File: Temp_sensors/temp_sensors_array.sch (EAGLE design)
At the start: 7 parts, among them U1 SI7021, U2 SI7021, U3 HDC1080, U4 HDC1080, U5 BME280, U6 BME280

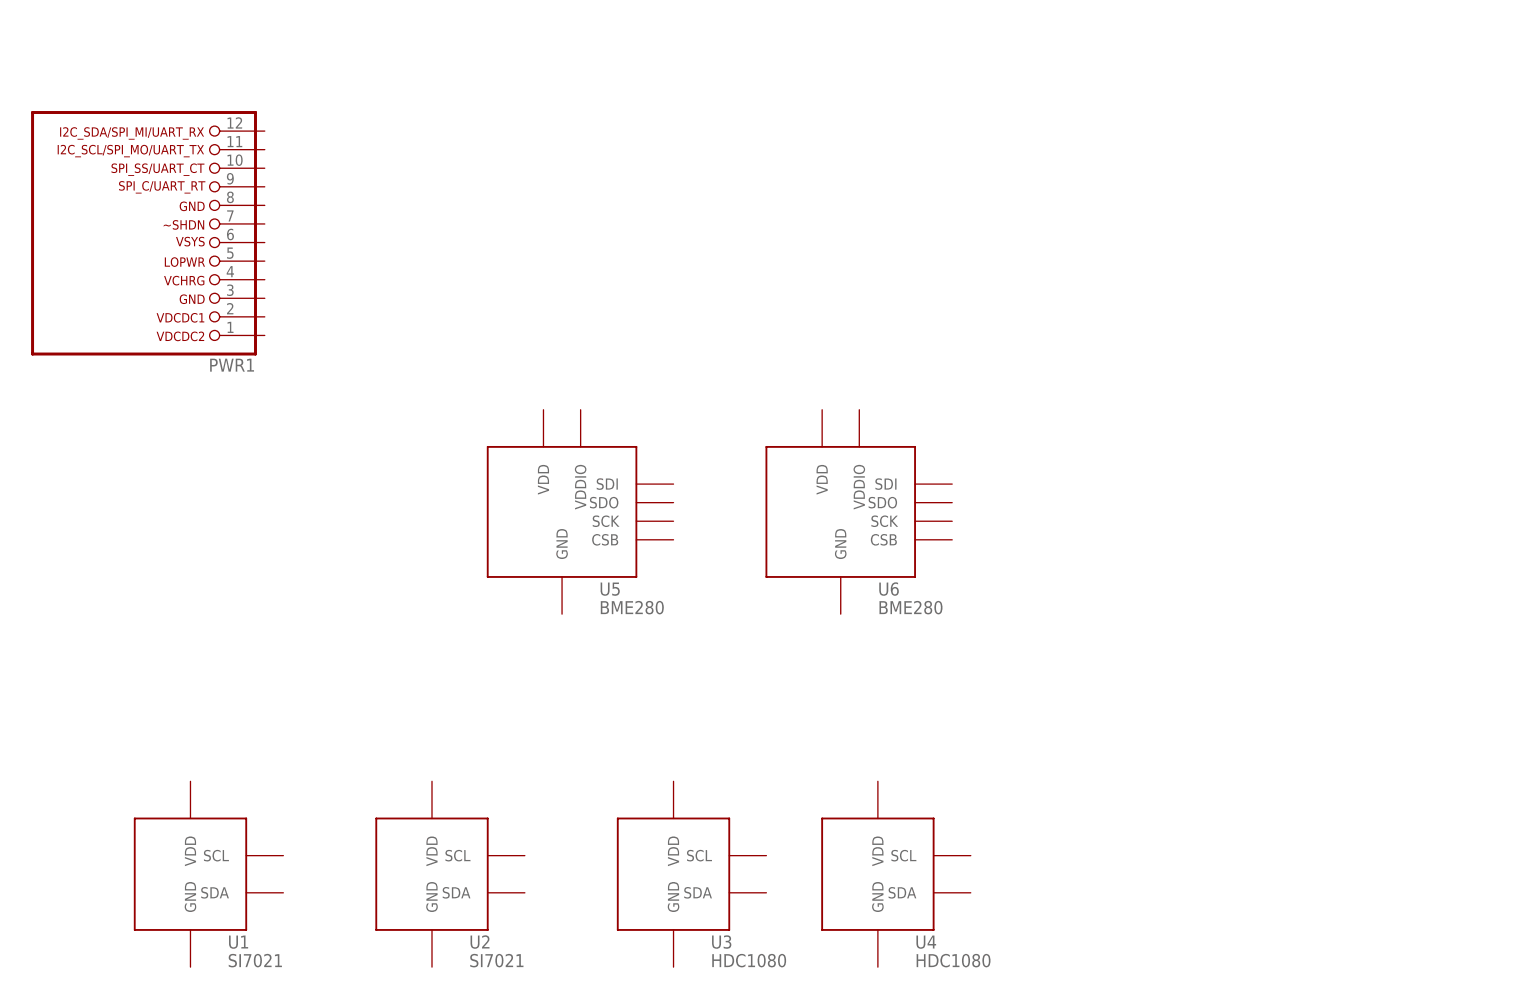
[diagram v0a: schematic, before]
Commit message: temp_array: added PCA9548APWR
Signed-off-by: malo <malo@25cmsquare.io>
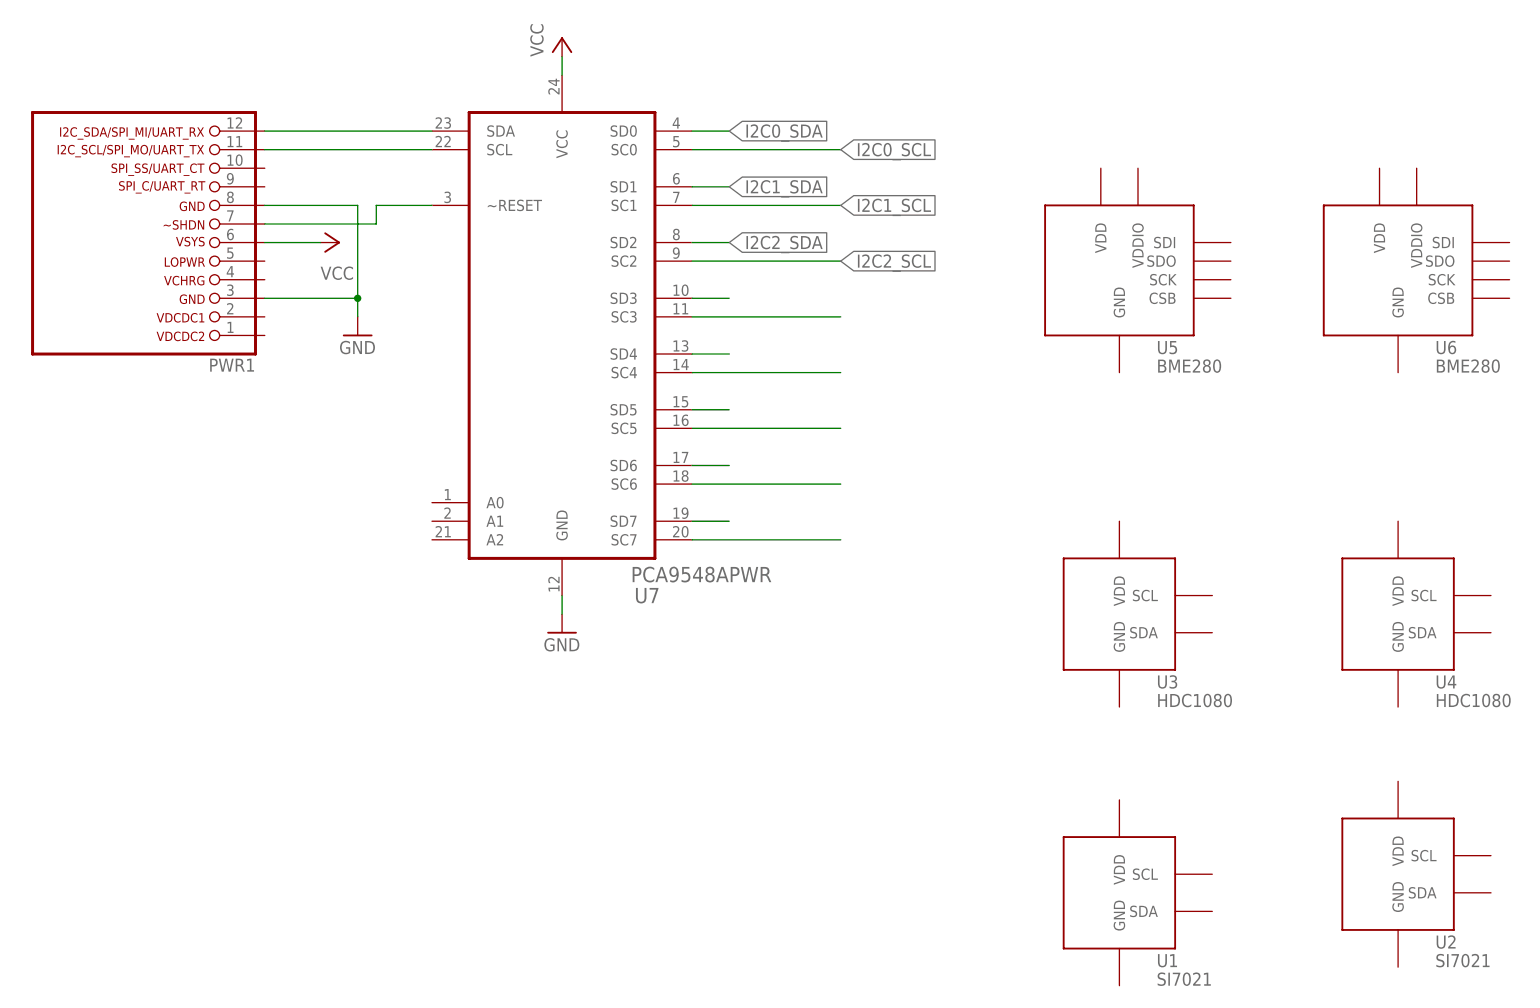
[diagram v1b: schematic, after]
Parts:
- added U7: PCA9548APWR, Texas Instruments_By_element14_Batch_1:PCA9548APWR
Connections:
- new net GND: PWR1.3, PWR1.8, U7.GND
- new net I2C0_SCL: U7.SC0
- new net I2C0_SDA: U7.SD0
- new net I2C1_SCL: U7.SC1
- new net I2C1_SDA: U7.SD1
- new net I2C2_SCL: U7.SC2
- new net I2C2_SDA: U7.SD2
- new net N$1: PWR1.12, U7.SDA
- new net N$10: U7.SD6
- new net N$11: U7.SC6
- new net N$12: U7.SD7
- new net N$13: U7.SC7
- new net N$2: PWR1.11, U7.SCL
- new net N$3: PWR1.7, U7.~RESET
- new net N$4: U7.SD3
- new net N$5: U7.SC3
- new net N$6: U7.SD4
- new net N$7: U7.SC4
- new net N$8: U7.SD5
- new net N$9: U7.SC5
- new net VCC: PWR1.6, U7.VCC
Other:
- moved on the sheet: U1, U2, U3, U4, U5, U6
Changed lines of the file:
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@@
 <part name="U5" library="25cmsquare" deviceset="BME280" device=""/>
 <part name="U6" library="25cmsquare" deviceset="BME280" device=""/>
+<part name="U7" library="Texas Instruments_By_element14_Batch_1" deviceset="PCA9548APWR" device=""/>
+<part name="GND1" library="supply1" deviceset="GND" device=""/>
+<part name="GND2" library="supply1" deviceset="GND" device=""/>
+<part name="P+1" library="supply1" deviceset="VCC" device=""/>
+<part name="P+2" library="supply1" deviceset="VCC" device=""/>
 </parts>
 <sheets>
@@
 </plain>
 <instances>
-<instance part="U1" gate="G$1" x="35.56" y="63.5"/>
-<instance part="U2" gate="G$1" x="68.58" y="63.5"/>
+<instance part="U1" gate="G$1" x="162.56" y="60.96"/>
+<instance part="U2" gate="G$1" x="200.66" y="63.5"/>
 <instance part="PWR1" gate="G$1" x="27.94" y="142.24" rot="R180"/>
 <instance part="FRAME1" gate="G$1" x="0" y="0"/>
-<instance part="U3" gate="G$1" x="101.6" y="55.88"/>
-<instance part="U4" gate="G$1" x="129.54" y="55.88"/>
-<instance part="U5" gate="G$1" x="78.74" y="96.52"/>
-<instance part="U6" gate="G$1" x="116.84" y="96.52"/>
+<instance part="U3" gate="G$1" x="162.56" y="91.44"/>
+<instance part="U4" gate="G$1" x="200.66" y="91.44"/>
+<instance part="U5" gate="G$1" x="154.94" y="129.54"/>
+<instance part="U6" gate="G$1" x="193.04" y="129.54"/>
+<instance part="U7" gate="A" x="86.36" y="129.54"/>
+<instance part="GND1" gate="1" x="58.42" y="129.54"/>
+<instance part="GND2" gate="1" x="86.36" y="88.9"/>
+<instance part="P+1" gate="VCC" x="86.36" y="170.18"/>
+<instance part="P+2" gate="VCC" x="55.88" y="142.24" smashed="yes" rot="R270">
+<attribute name="VALUE" x="53.34" y="137.16" size="1.778" layer="96"/>
+</instance>
 </instances>
 <busses>
 </busses>
 <nets>
+<net name="N$1" class="0">
+<segment>
+<pinref part="PWR1" gate="G$1" pin="12"/>
+<pinref part="U7" gate="A" pin="SDA"/>
+<wire x1="45.72" y1="157.48" x2="68.58" y2="157.48" width="0.1524" layer="91"/>
+</segment>
+</net>
+<net name="N$2" class="0">
+<segment>
+<pinref part="PWR1" gate="G$1" pin="11"/>
+<pinref part="U7" gate="A" pin="SCL"/>
+<wire x1="45.72" y1="154.94" x2="68.58" y2="154.94" width="0.1524" layer="91"/>
+</segment>
+</net>
+<net name="N$3" class="0">
+<segment>
+<pinref part="PWR1" gate="G$1" pin="7"/>
+<wire x1="45.72" y1="144.78" x2="60.96" y2="144.78" width="0.1524" layer="91"/>
+<wire x1="60.96" y1="144.78" x2="60.96" y2="147.32" width="0.1524" layer="91"/>
+<pinref part="U7" gate="A" pin="~RESET"/>
+<wire x1="60.96" y1="147.32" x2="68.58" y2="147.32" width="0.1524" layer="91"/>
+</segment>
+</net>
+<net name="GND" class="0">
+<segment>
+<pinref part="PWR1" gate="G$1" pin="3"/>
+<wire x1="45.72" y1="134.62" x2="58.42" y2="134.62" width="0.1524" layer="91"/>
+<wire x1="58.42" y1="134.62" x2="58.42" y2="132.08" width="0.1524" layer="91"/>
+<pinref part="GND1" gate="1" pin="GND"/>
+<pinref part="PWR1" gate="G$1" pin="8"/>
+<wire x1="45.72" y1="147.32" x2="58.42" y2="147.32" width="0.1524" layer="91"/>
+<wire x1="58.42" y1="147.32" x2="58.42" y2="134.62" width="0.1524" layer="91"/>
+<junction x="58.42" y="134.62"/>
+</segment>
+<segment>
+<pinref part="U7" gate="A" pin="GND"/>
+<pinref part="GND2" gate="1" pin="GND"/>
+<wire x1="86.36" y1="93.98" x2="86.36" y2="91.44" width="0.1524" layer="91"/>
+</segment>
+</net>
+<net name="VCC" class="0">
+<segment>
+<pinref part="PWR1" gate="G$1" pin="6"/>
+<pinref part="P+2" gate="VCC" pin="VCC"/>
+<wire x1="45.72" y1="142.24" x2="53.34" y2="142.24" width="0.1524" layer="91"/>
+</segment>
+<segment>
+<pinref part="U7" gate="A" pin="VCC"/>
+<pinref part="P+1" gate="VCC" pin="VCC"/>
+<wire x1="86.36" y1="165.1" x2="86.36" y2="167.64" width="0.1524" layer="91"/>
+</segment>
+</net>
+<net name="I2C0_SDA" class="0">
+<segment>
+<pinref part="U7" gate="A" pin="SD0"/>
+<wire x1="104.14" y1="157.48" x2="109.22" y2="157.48" width="0.1524" layer="91"/>
+<label x="109.22" y="157.48" size="1.778" layer="95" xref="yes"/>
+</segment>
+</net>
+<net name="I2C0_SCL" class="0">
+<segment>
+<pinref part="U7" gate="A" pin="SC0"/>
+<wire x1="104.14" y1="154.94" x2="124.46" y2="154.94" width="0.1524" layer="91"/>
+<label x="124.46" y="154.94" size="1.778" layer="95" xref="yes"/>
+</segment>
+</net>
+<net name="I2C1_SDA" class="0">
+<segment>
+<pinref part="U7" gate="A" pin="SD1"/>
+<wire x1="104.14" y1="149.86" x2="109.22" y2="149.86" width="0.1524" layer="91"/>
+<label x="109.22" y="149.86" size="1.778" layer="95" xref="yes"/>
+</segment>
+</net>
+<net name="I2C1_SCL" class="0">
+<segment>
+<pinref part="U7" gate="A" pin="SC1"/>
+<wire x1="104.14" y1="147.32" x2="124.46" y2="147.32" width="0.1524" layer="91"/>
+<label x="124.46" y="147.32" size="1.778" layer="95" xref="yes"/>
+</segment>
+</net>
+<net name="I2C2_SDA" class="0">
+<segment>
+<pinref part="U7" gate="A" pin="SD2"/>
+<wire x1="104.14" y1="142.24" x2="109.22" y2="142.24" width="0.1524" layer="91"/>
+<label x="109.22" y="142.24" size="1.778" layer="95" xref="yes"/>
+</segment>
+</net>
+<net name="I2C2_SCL" class="0">
+<segment>
+<pinref part="U7" gate="A" pin="SC2"/>
+<wire x1="104.14" y1="139.7" x2="124.46" y2="139.7" width="0.1524" layer="91"/>
+<label x="124.46" y="139.7" size="1.778" layer="95" xref="yes"/>
+</segment>
+</net>
+<net name="N$4" class="0">
+<segment>
+<pinref part="U7" gate="A" pin="SD3"/>
+<wire x1="104.14" y1="134.62" x2="109.22" y2="134.62" width="0.1524" layer="91"/>
+</segment>
+</net>
+<net name="N$5" class="0">
+<segment>
+<pinref part="U7" gate="A" pin="SC3"/>
+<wire x1="104.14" y1="132.08" x2="124.46" y2="132.08" width="0.1524" layer="91"/>
+</segment>
+</net>
+<net name="N$6" class="0">
+<segment>
+<pinref part="U7" gate="A" pin="SD4"/>
+<wire x1="104.14" y1="127" x2="109.22" y2="127" width="0.1524" layer="91"/>
+</segment>
+</net>
+<net name="N$7" class="0">
+<segment>
+<pinref part="U7" gate="A" pin="SC4"/>
+<wire x1="104.14" y1="124.46" x2="124.46" y2="124.46" width="0.1524" layer="91"/>
+</segment>
+</net>
+<net name="N$8" class="0">
+<segment>
+<pinref part="U7" gate="A" pin="SD5"/>
+<wire x1="104.14" y1="119.38" x2="109.22" y2="119.38" width="0.1524" layer="91"/>
+</segment>
+</net>
+<net name="N$9" class="0">
+<segment>
+<pinref part="U7" gate="A" pin="SC5"/>
+<wire x1="104.14" y1="116.84" x2="124.46" y2="116.84" width="0.1524" layer="91"/>
+</segment>
+</net>
+<net name="N$10" class="0">
+<segment>
+<pinref part="U7" gate="A" pin="SD6"/>
+<wire x1="104.14" y1="111.76" x2="109.22" y2="111.76" width="0.1524" layer="91"/>
+</segment>
+</net>
+<net name="N$11" class="0">
+<segment>
+<pinref part="U7" gate="A" pin="SC6"/>
+<wire x1="104.14" y1="109.22" x2="124.46" y2="109.22" width="0.1524" layer="91"/>
+</segment>
+</net>
+<net name="N$12" class="0">
+<segment>
+<pinref part="U7" gate="A" pin="SD7"/>
+<wire x1="104.14" y1="104.14" x2="109.22" y2="104.14" width="0.1524" layer="91"/>
+</segment>
+</net>
+<net name="N$13" class="0">
+<segment>
+<pinref part="U7" gate="A" pin="SC7"/>
+<wire x1="104.14" y1="101.6" x2="124.46" y2="101.6" width="0.1524" layer="91"/>
+</segment>
+</net>
 </nets>
 </sheet>
